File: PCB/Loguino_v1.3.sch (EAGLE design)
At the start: 47 parts, among them X1 22-23-2041, X4 22-23-2041, X5 22-23-2021

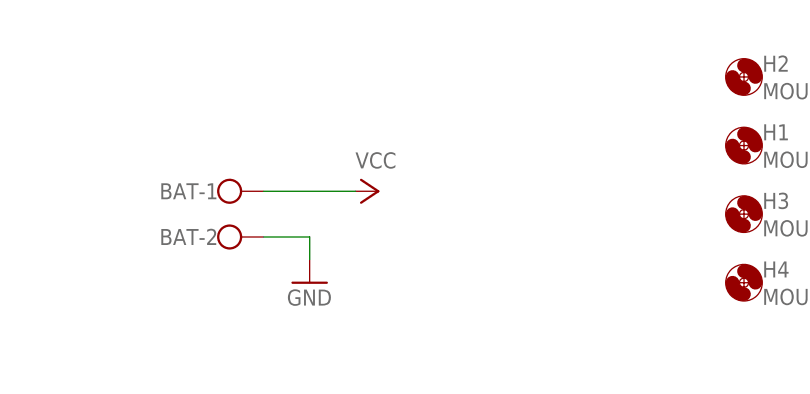
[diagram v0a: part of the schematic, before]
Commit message: updated PCB and sketches to v1.3
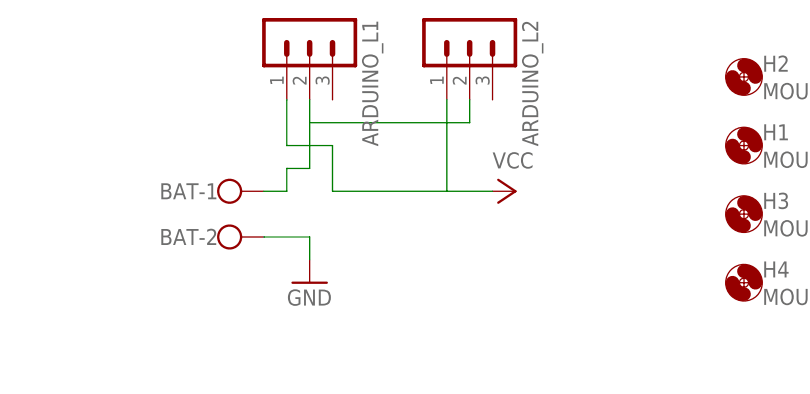
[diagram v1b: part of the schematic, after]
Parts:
- added ARDUINO_L1, ARDUINO_L2: (no value), con-lstb:MA03-1
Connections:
- new net N$1: ARDUINO_L1.2, ARDUINO_L2.2, BAT-1.KL
- net VCC: now also ARDUINO_L1.1, ARDUINO_L2.1; no longer BAT-1.KL
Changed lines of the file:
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@@
 <part name="R12" library="resistor" deviceset="R-EU_" device="0207/10" value="2.2K"/>
 <part name="R13" library="resistor" deviceset="R-EU_" device="0207/10" value="2.2K"/>
+<part name="ARDUINO_L1" library="con-lstb" deviceset="MA03-1" device=""/>
+<part name="ARDUINO_L2" library="con-lstb" deviceset="MA03-1" device=""/>
 </parts>
 <sheets>
@@
 <instance part="BAT" gate="-1" x="35.56" y="162.56"/>
 <instance part="BAT" gate="-2" x="35.56" y="157.48"/>
-<instance part="P+5" gate="VCC" x="53.34" y="162.56" rot="R270"/>
+<instance part="P+5" gate="VCC" x="68.58" y="162.56" rot="R270"/>
 <instance part="I2C" gate="-1" x="-96.52" y="20.32" rot="R180"/>
 <instance part="I2C" gate="-2" x="-96.52" y="22.86" rot="R180"/>
@@
 <instance part="R12" gate="G$1" x="-66.04" y="106.68"/>
 <instance part="R13" gate="G$1" x="-66.04" y="101.6"/>
+<instance part="ARDUINO_L1" gate="G$1" x="45.72" y="180.34" rot="R270"/>
+<instance part="ARDUINO_L2" gate="G$1" x="63.5" y="180.34" rot="R270"/>
 </instances>
 <busses>
@@
 </segment>
 <segment>
-<pinref part="BAT" gate="-1" pin="KL"/>
-<pinref part="P+5" gate="VCC" pin="VCC"/>
-<wire x1="40.64" y1="162.56" x2="50.8" y2="162.56" width="0.1524" layer="91"/>
-</segment>
-<segment>
 <pinref part="I2C" gate="-3" pin="S"/>
 <wire x1="-93.98" y1="25.4" x2="-86.36" y2="25.4" width="0.1524" layer="91"/>
@@
 <pinref part="P+4" gate="VCC" pin="VCC"/>
 <wire x1="-152.4" y1="93.98" x2="-154.94" y2="93.98" width="0.1524" layer="91"/>
+</segment>
+<segment>
+<pinref part="P+5" gate="VCC" pin="VCC"/>
+<wire x1="60.96" y1="162.56" x2="66.04" y2="162.56" width="0.1524" layer="91"/>
+<pinref part="ARDUINO_L2" gate="G$1" pin="1"/>
+<wire x1="60.96" y1="162.56" x2="60.96" y2="172.72" width="0.1524" layer="91"/>
+<wire x1="60.96" y1="162.56" x2="48.26" y2="162.56" width="0.1524" layer="91"/>
+<wire x1="48.26" y1="162.56" x2="48.26" y2="167.64" width="0.1524" layer="91"/>
+<pinref part="ARDUINO_L1" gate="G$1" pin="1"/>
+<wire x1="48.26" y1="167.64" x2="43.18" y2="167.64" width="0.1524" layer="91"/>
+<wire x1="43.18" y1="167.64" x2="43.18" y2="172.72" width="0.1524" layer="91"/>
 </segment>
 </net>
@@
 </segment>
 </net>
+<net name="N$1" class="0">
+<segment>
+<pinref part="BAT" gate="-1" pin="KL"/>
+<wire x1="40.64" y1="162.56" x2="43.18" y2="162.56" width="0.1524" layer="91"/>
+<wire x1="43.18" y1="162.56" x2="43.18" y2="165.1" width="0.1524" layer="91"/>
+<pinref part="ARDUINO_L1" gate="G$1" pin="2"/>
+<wire x1="43.18" y1="165.1" x2="45.72" y2="165.1" width="0.1524" layer="91"/>
+<wire x1="45.72" y1="165.1" x2="45.72" y2="170.18" width="0.1524" layer="91"/>
+<wire x1="45.72" y1="172.72" x2="45.72" y2="170.18" width="0.1524" layer="91"/>
+<pinref part="ARDUINO_L2" gate="G$1" pin="2"/>
+<wire x1="45.72" y1="170.18" x2="63.5" y2="170.18" width="0.1524" layer="91"/>
+<wire x1="63.5" y1="170.18" x2="63.5" y2="172.72" width="0.1524" layer="91"/>
+</segment>
+</net>
